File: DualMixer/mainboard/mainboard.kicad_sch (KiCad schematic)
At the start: 62 parts, among them J1 IN_A1, J10 IN_B4, J11 OUTB, J12 Conn_02x05_Odd_Even, J13 Conn_01x03_Male, J2 IN_A2, J3 IN_A3, J4 OUTA, J5 Conn_02x06_Odd_Even, J6 IN_A4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

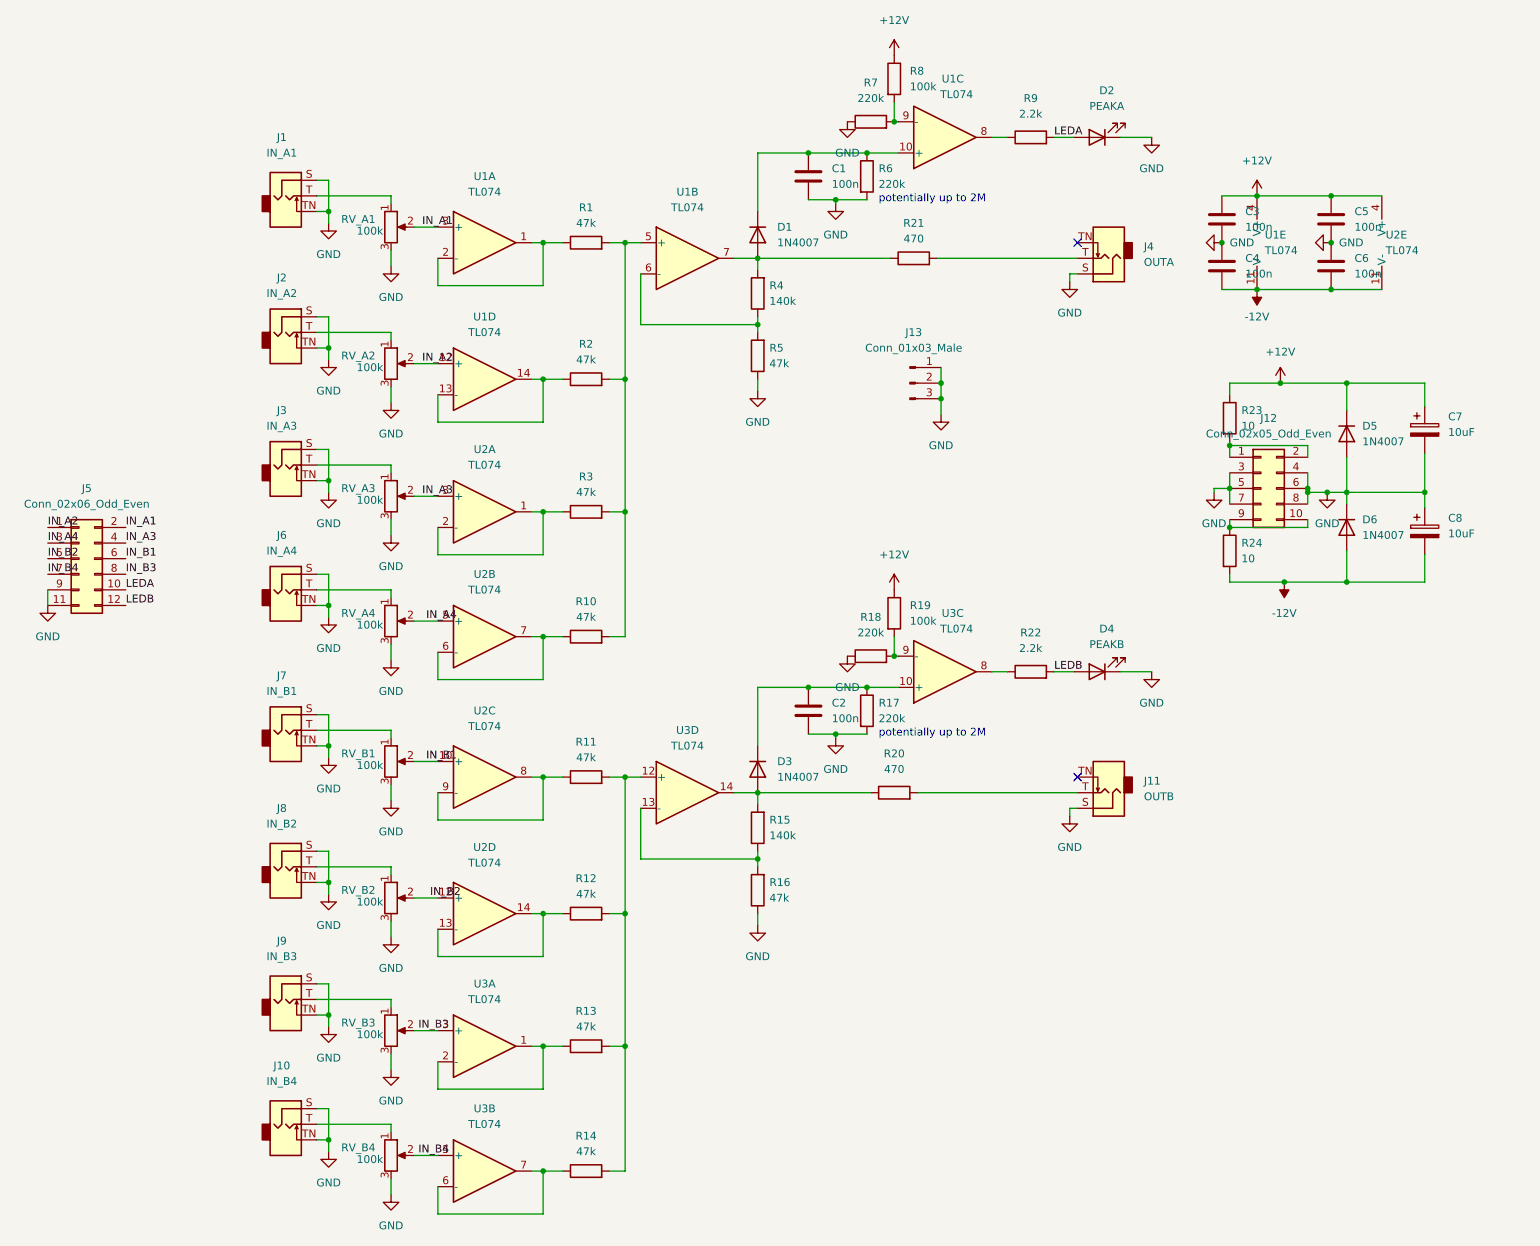
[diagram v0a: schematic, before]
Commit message: Add missing output connectors to IO board
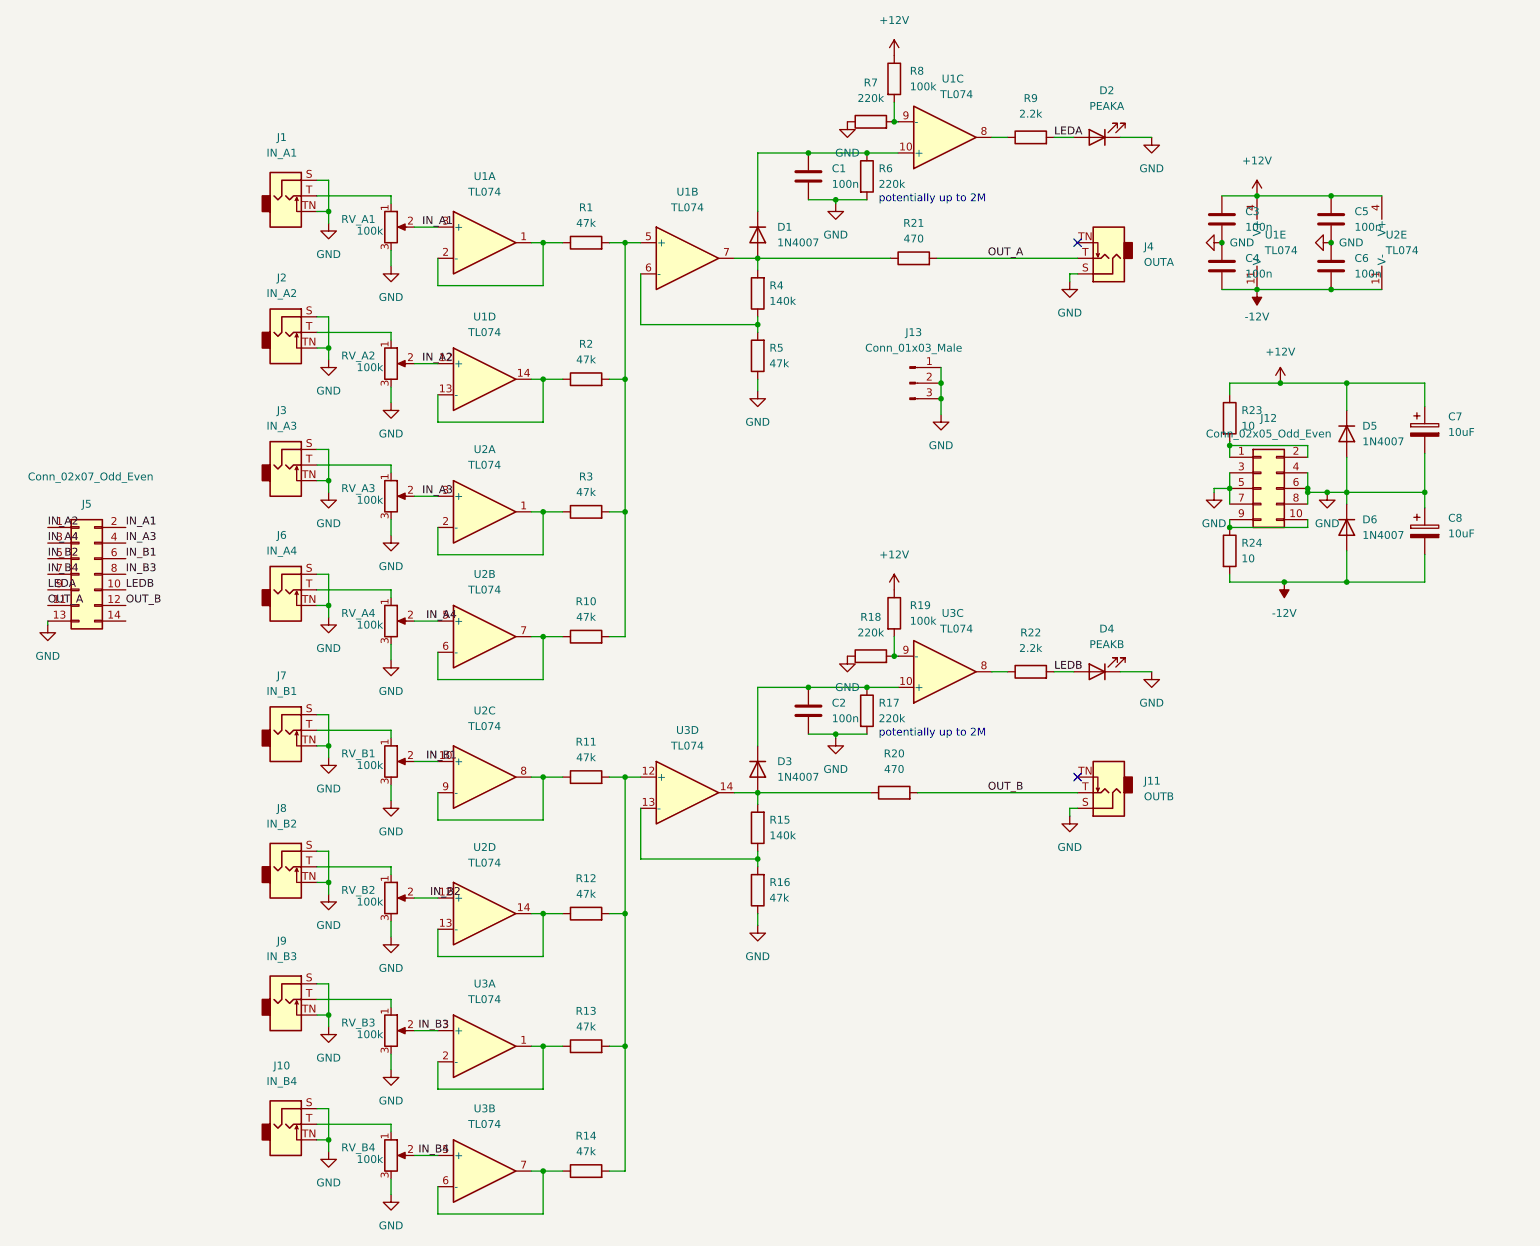
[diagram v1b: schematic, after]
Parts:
- J5: value Conn_02x06_Odd_Even -> Conn_02x07_Odd_Even; footprint Connector_PinHeader_2.54mm:PinHeader_2x06_P2.54mm_Vertical -> Connector_PinHeader_2.54mm:PinHeader_2x07_P2.54mm_Vertical; symbol Connector_Generic:Conn_02x06_Odd_Even -> Connector_Generic:Conn_02x07_Odd_Even
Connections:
- net GND: now also J5.13 (Pin_13); no longer J5.11 (Pin_11), J5.9 (Pin_9)
- net LEDA: now also J5.9 (Pin_9); no longer J5.10 (Pin_10)
- net LEDB: now also J5.10 (Pin_10); no longer J5.12 (Pin_12)
- net OUT_A: now reaches J4.T, R21.2
- net OUT_A: now also J5.11 (Pin_11)
- net OUT_B: now reaches J11.T, R20.2
- net OUT_B: now also J5.12 (Pin_12)
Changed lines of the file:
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@@
-    (stroke (width 0) (type default) (color 0 0 0 0))
-  )
-  (wire (pts (xy 32.385 109.22) (xy 32.385 111.76))
     (stroke (width 0) (type default) (color 0 0 0 0))
   )
@@
     (stroke (width 0) (type default) (color 0 0 0 0))
   )
+  (wire (pts (xy 32.385 114.3) (xy 32.385 114.935))
+    (stroke (width 0) (type default) (color 0 0 0 0))
+  )
   (wire (pts (xy 113.03 203.835) (xy 116.205 203.835))
     (stroke (width 0) (type default) (color 0 0 0 0))
@@
     (effects (font (size 1.27 1.27)) (justify left bottom))
   )
+  (label "OUT_A" (at 32.385 111.76 0)
+    (effects (font (size 1.27 1.27)) (justify left bottom))
+  )
   (label "LEDA" (at 196.215 35.56 0)
     (effects (font (size 1.27 1.27)) (justify left bottom))
@@
     (effects (font (size 1.27 1.27)) (justify left bottom))
   )
-  (label "LEDB" (at 45.085 111.76 0)
+  (label "OUT_B" (at 185.42 142.24 0)
+    (effects (font (size 1.27 1.27)) (justify left bottom))
+  )
+  (label "LEDB" (at 45.085 109.22 0)
     (effects (font (size 1.27 1.27)) (justify left bottom))
   )
@@
     (effects (font (size 1.27 1.27)) (justify left bottom))
   )
+  (label "OUT_A" (at 185.42 55.245 0)
+    (effects (font (size 1.27 1.27)) (justify left bottom))
+  )
   (label "IN_B1" (at 45.085 104.14 0)
     (effects (font (size 1.27 1.27)) (justify left bottom))
@@
     (effects (font (size 1.27 1.27)) (justify left bottom))
   )
-  (label "LEDA" (at 45.085 109.22 0)
+  (label "LEDA" (at 32.385 109.22 0)
     (effects (font (size 1.27 1.27)) (justify left bottom))
   )
@@
   )
   (label "IN_A2" (at 32.385 99.06 0)
+    (effects (font (size 1.27 1.27)) (justify left bottom))
+  )
+  (label "OUT_B" (at 45.085 111.76 0)
     (effects (font (size 1.27 1.27)) (justify left bottom))
   )
@@
     (pin "1")
   )
-  (symbol (lib_id "Connector_Generic:Conn_02x06_Odd_Even") (at 37.465 104.14 0) (unit 1)
-    (in_bom yes) (on_board yes) (fields_autoplaced)
-    (property "Reference" "J5" (id 0) (at 38.735 92.71 0))
-    (property "Value" "Conn_02x06_Odd_Even" (id 1) (at 38.735 95.25 0))
-    (property "Footprint" "Connector_PinHeader_2.54mm:PinHeader_2x06_P2.54mm_Vertical" (id 2) (at 37.465 104.14 0)
-      (effects (font (size 1.27 1.27)) hide)
-    )
-    (property "Datasheet" "~" (id 3) (at 37.465 104.14 0)
+  (symbol (lib_id "Connector_Generic:Conn_02x07_Odd_Even") (at 37.465 106.68 0) (unit 1)
+    (in_bom yes) (on_board yes)
+    (property "Reference" "J5" (id 0) (at 38.735 95.25 0))
+    (property "Value" "Conn_02x07_Odd_Even" (id 1) (at 39.37 90.805 0))
+    (property "Footprint" "Connector_PinHeader_2.54mm:PinHeader_2x07_P2.54mm_Vertical" (id 2) (at 37.465 106.68 0)
+      (effects (font (size 1.27 1.27)) hide)
+    )
+    (property "Datasheet" "~" (id 3) (at 37.465 106.68 0)
       (effects (font (size 1.27 1.27)) hide)
     )
@@
     (pin "11")
     (pin "12")
+    (pin "13")
+    (pin "14")
     (pin "2")
     (pin "3")
@@
     (pin "1")
   )
-  (symbol (lib_id "power:GND") (at 32.385 111.76 0) (unit 1)
-    (in_bom yes) (on_board yes) (fields_autoplaced)
-    (property "Reference" "#PWR0119" (id 0) (at 32.385 118.11 0)
-      (effects (font (size 1.27 1.27)) hide)
-    )
-    (property "Value" "GND" (id 1) (at 32.385 116.84 0))
-    (property "Footprint" "" (id 2) (at 32.385 111.76 0)
-      (effects (font (size 1.27 1.27)) hide)
-    )
-    (property "Datasheet" "" (id 3) (at 32.385 111.76 0)
+  (symbol (lib_id "power:GND") (at 32.385 114.935 0) (unit 1)
+    (in_bom yes) (on_board yes) (fields_autoplaced)
+    (property "Reference" "#PWR0119" (id 0) (at 32.385 121.285 0)
+      (effects (font (size 1.27 1.27)) hide)
+    )
+    (property "Value" "GND" (id 1) (at 32.385 120.015 0))
+    (property "Footprint" "" (id 2) (at 32.385 114.935 0)
+      (effects (font (size 1.27 1.27)) hide)
+    )
+    (property "Datasheet" "" (id 3) (at 32.385 114.935 0)
       (effects (font (size 1.27 1.27)) hide)
     )
@@
     )
     (path "/6f7241f2-2fde-4654-bbfb-b1261b5673b6"
-      (reference "J5") (unit 1) (value "Conn_02x06_Odd_Even") (footprint "Connector_PinHeader_2.54mm:PinHeader_2x06_P2.54mm_Vertical")
+      (reference "J5") (unit 1) (value "Conn_02x07_Odd_Even") (footprint "Connector_PinHeader_2.54mm:PinHeader_2x07_P2.54mm_Vertical")
     )
     (path "/44412da0-dbc9-4b0b-8241-a43103e198f6"

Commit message: Split up into mainboard and ioboard
And do routing for mainboard
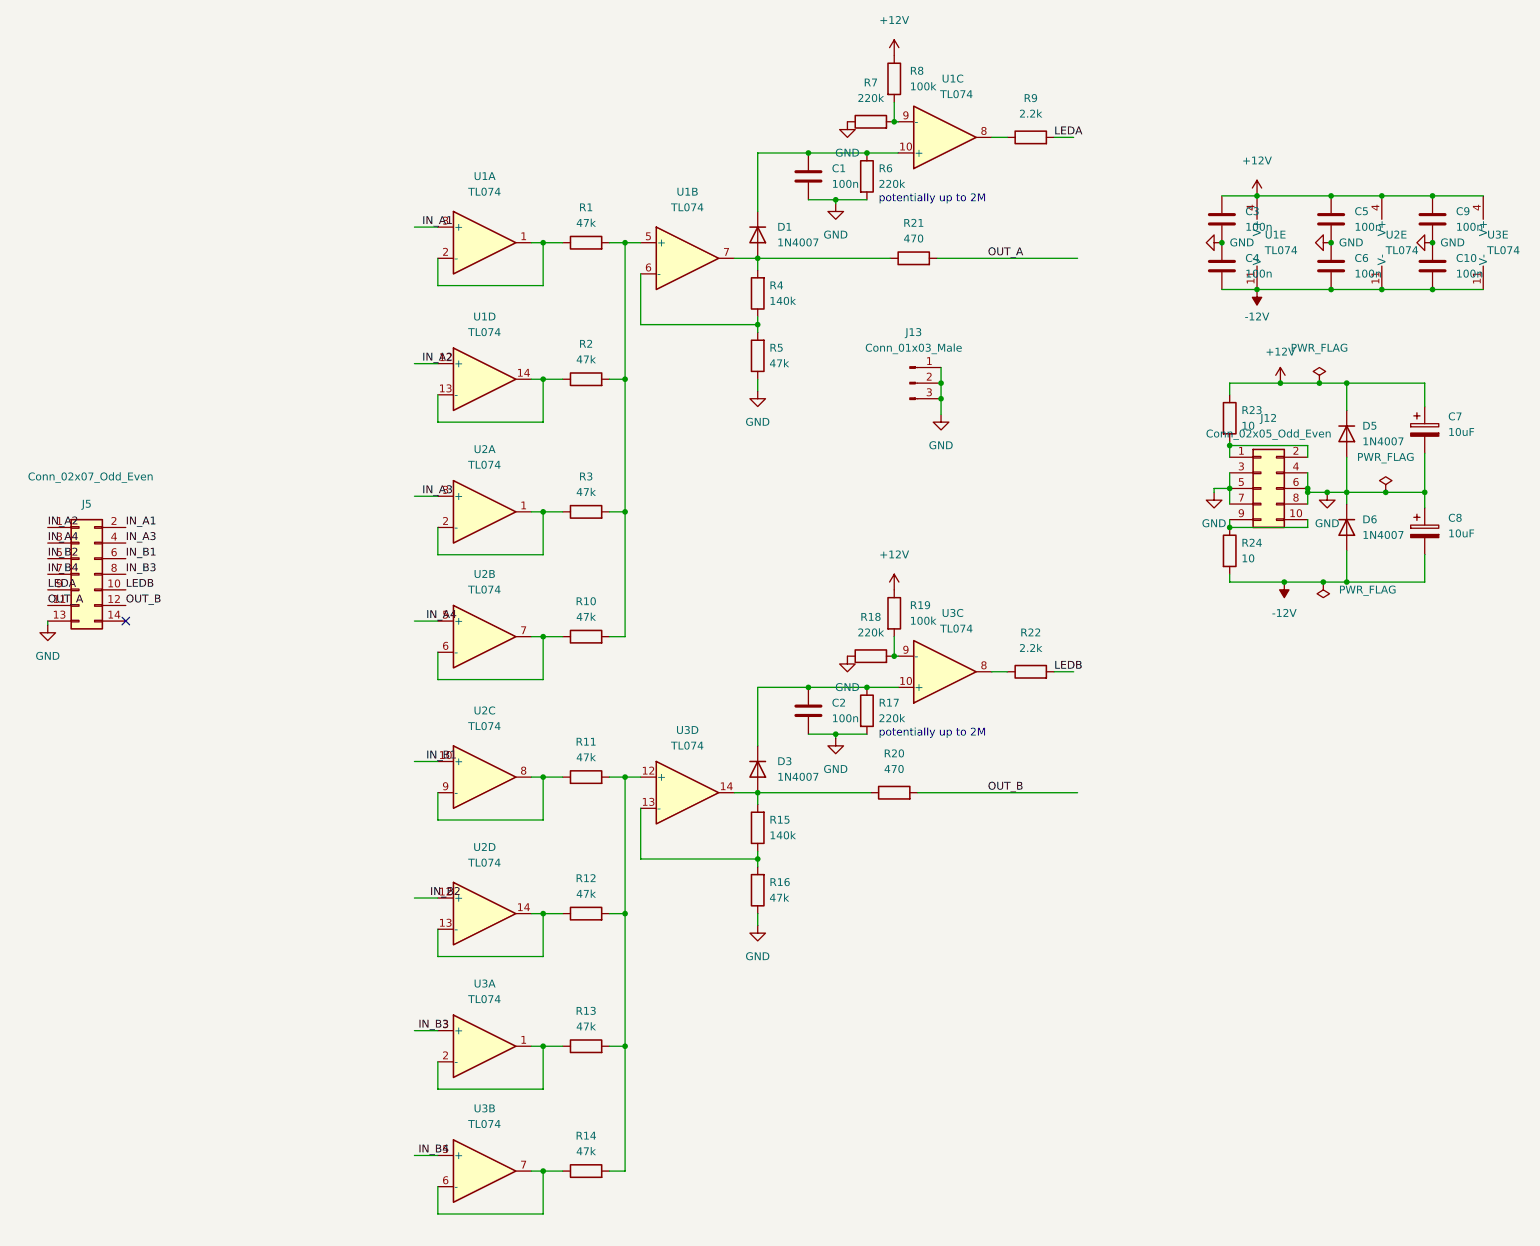
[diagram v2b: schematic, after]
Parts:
- removed D2: PEAKA, LED_THT:LED_D3.0mm, symbol Device:LED
- removed D4: PEAKB, LED_THT:LED_D3.0mm, symbol Device:LED
- removed J1: IN_A1, Connector_Audio:Jack_3.5mm_QingPu_WQP-PJ398SM_Vertical_CircularHoles, symbol Connector:AudioJack2_SwitchT
- removed J10: IN_B4, Connector_Audio:Jack_3.5mm_QingPu_WQP-PJ398SM_Vertical_CircularHoles, symbol Connector:AudioJack2_SwitchT
- removed J11: OUTB, Connector_Audio:Jack_3.5mm_QingPu_WQP-PJ398SM_Vertical_CircularHoles, symbol Connector:AudioJack2_SwitchT
- removed J2: IN_A2, Connector_Audio:Jack_3.5mm_QingPu_WQP-PJ398SM_Vertical_CircularHoles, symbol Connector:AudioJack2_SwitchT
- removed J3: IN_A3, Connector_Audio:Jack_3.5mm_QingPu_WQP-PJ398SM_Vertical_CircularHoles, symbol Connector:AudioJack2_SwitchT
- removed J4: OUTA, Connector_Audio:Jack_3.5mm_QingPu_WQP-PJ398SM_Vertical_CircularHoles, symbol Connector:AudioJack2_SwitchT
- removed J6: IN_A4, Connector_Audio:Jack_3.5mm_QingPu_WQP-PJ398SM_Vertical_CircularHoles, symbol Connector:AudioJack2_SwitchT
- removed J7: IN_B1, Connector_Audio:Jack_3.5mm_QingPu_WQP-PJ398SM_Vertical_CircularHoles, symbol Connector:AudioJack2_SwitchT
- removed J8: IN_B2, Connector_Audio:Jack_3.5mm_QingPu_WQP-PJ398SM_Vertical_CircularHoles, symbol Connector:AudioJack2_SwitchT
- removed J9: IN_B3, Connector_Audio:Jack_3.5mm_QingPu_WQP-PJ398SM_Vertical_CircularHoles, symbol Connector:AudioJack2_SwitchT
- removed RV_A1, RV_A2, RV_A3, RV_A4, RV_B1, RV_B2, RV_B3, RV_B4: 100k, Potentiometer_THT:Potentiometer_Alps_RK09K_Single_Vertical, symbol Device:R_Potentiometer
- added C10, C9: 100n, Capacitor_SMD:C_0603_1608Metric_Pad1.08x0.95mm_HandSolder, symbol Device:C
- added unit 5 of U3
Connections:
- net +12V: now also C9.1, U3.4 (V+)
- net -12V: now also C10.2, U3.11 (V-)
- net GND: now also C10.1, C9.2
- no-connect marks 2 -> 1

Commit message: Apply fixes for DualMixer rev1 module
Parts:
- R18, R7: value 220k -> 33k
